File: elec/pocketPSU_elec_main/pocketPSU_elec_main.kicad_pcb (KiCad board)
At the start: 2 copper layers, 90 x 90 mm, 76 parts, among them J1 Header-Male-2.54_1x20, J2 Conn_01x03_Pin, J3 Conn_01x12_Pin, SW1 EC11E09244BS, SW3 TS-1187A-B-A-B, SW6 TS-1187A-B-A-B, U1 2N7002_C5224215, U2 ESP32-S3-WROOM-1(N16R2), U3 AMS1117-3.3, U4 FUSB302MPX, U5 F.0603.00026/P2-0603B1TS2-06T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

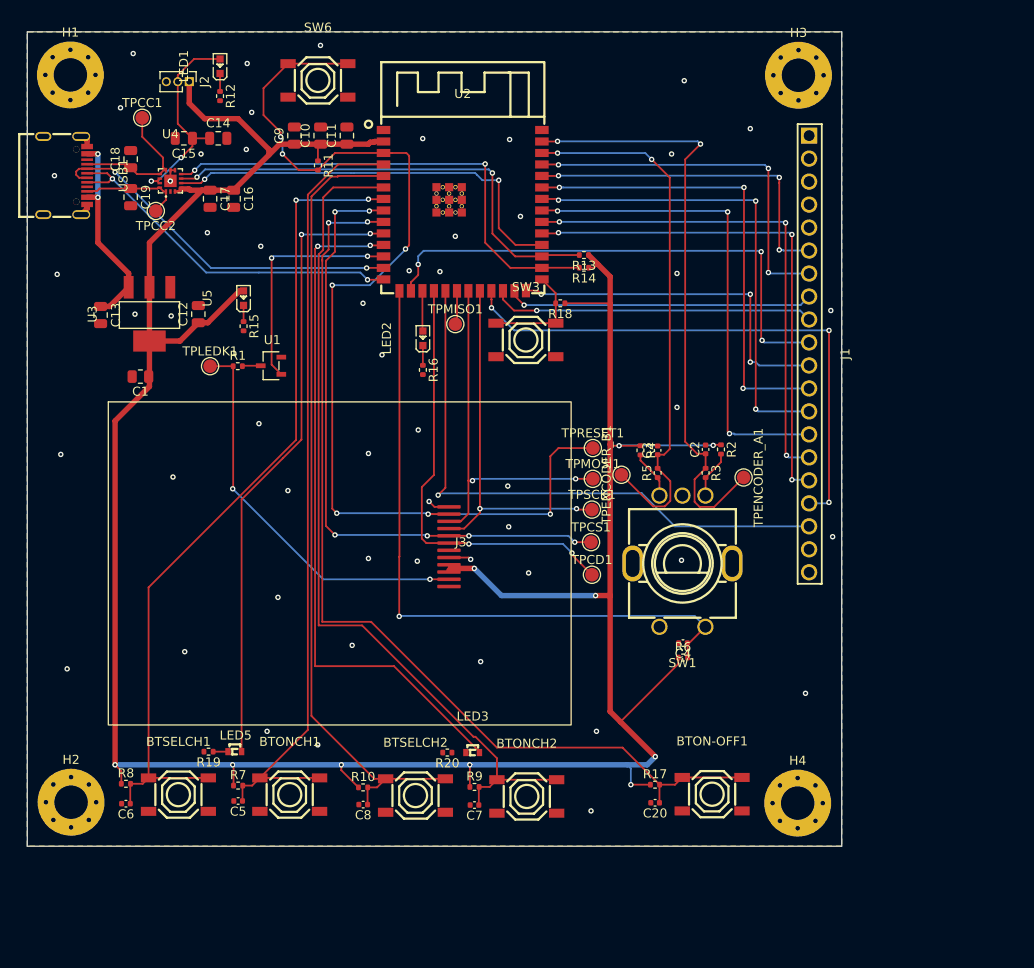
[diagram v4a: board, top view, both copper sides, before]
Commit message: Cleanup, Buck, CAN (#6)
* mid-layout

* finished routing

* Kibot (#7)

Add kibot with JLC output generation

* fix 3d, add drc

* fix erc

* fix pcb drc

* drc ignore_unconnected

* attempt to add githash and tag

* add silk githash string

* add silk tag string

* change outputs

---------

Co-authored-by: Jarrod Tuma <jtuma@Jarrods-Laptop.local>
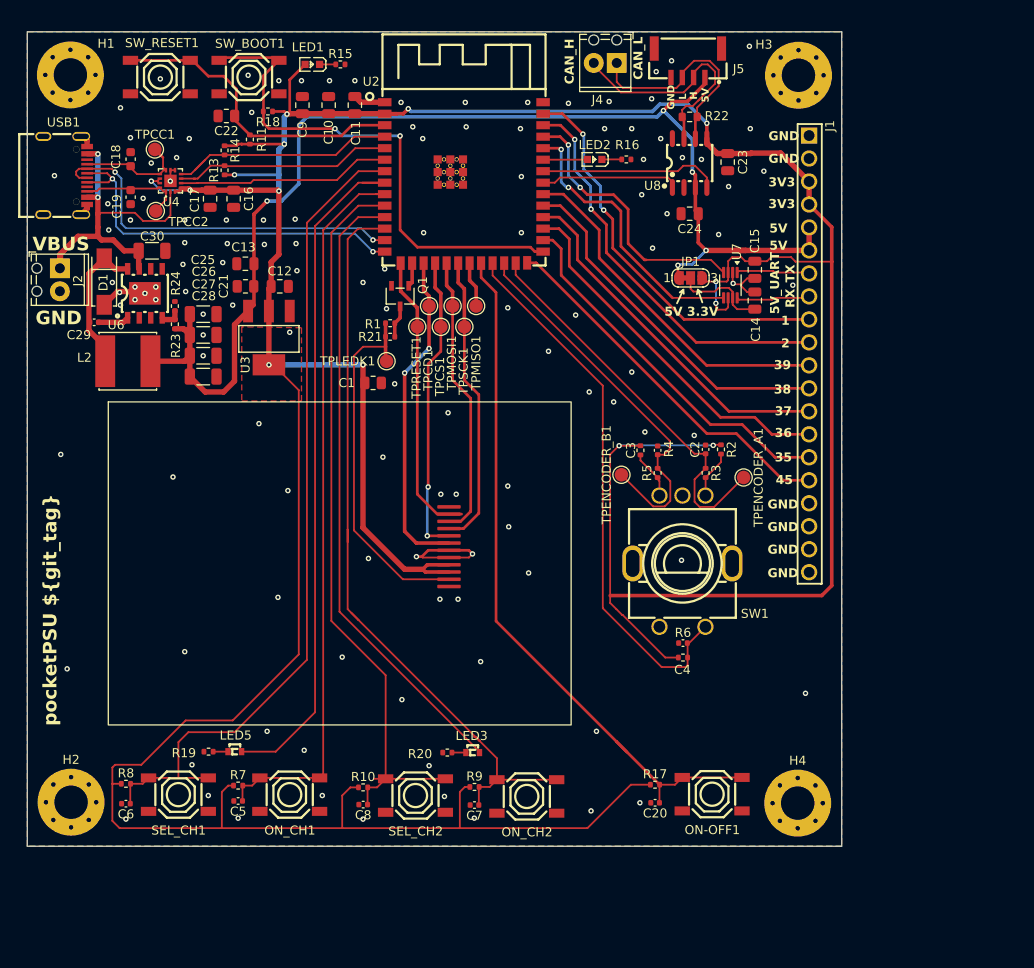
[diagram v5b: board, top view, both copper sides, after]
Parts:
- removed the LED1 at (118.9, 39.5)
- removed R12: 100R, Resistor_SMD:R_0402_1005Metric
- added C21: 1uF, Resistor_SMD:R_0805_2012Metric, F.Cu at (121.7, 63.8)
- added C22: 1uF, Resistor_SMD:R_0805_2012Metric, F.Cu at (119.6, 45.0)
- added C23: 100nF, Capacitor_SMD:C_0805_2012Metric, F.Cu at (175.0, 50.1)
- added C24: 100nF, Capacitor_SMD:C_0805_2012Metric, F.Cu at (170.8, 55.8)
- added C25: 47uF, Capacitor_SMD:C_1206_3216Metric, F.Cu at (117.0, 66.9)
- added C26: 47uF, Capacitor_SMD:C_1206_3216Metric, F.Cu at (117.0, 69.2)
- added C27: 47uF, Capacitor_SMD:C_1206_3216Metric, F.Cu at (117.0, 71.5)
- added C28: 47uF, Capacitor_SMD:C_1206_3216Metric, F.Cu at (117.0, 73.8)
- added C29: 10nF, Capacitor_SMD:C_0402_1005Metric, F.Cu at (105.0, 67.8)
- added C30: 4.7uF, Capacitor_SMD:C_1206_3216Metric, F.Cu at (111.4, 59.9)
- added D1: SS14, footprints:SMA_L4.2-W2.6-LS5.3-RD, F.Cu at (106.1, 63.3)
- added J4: Screw_Terminal_01x02, TerminalBlock_Phoenix:TerminalBlock_Phoenix_MPT-0,5-2-2.54_1x02_P2.54mm_Horizontal, F.Cu at (162.7, 39.1)
- added J5: SM04B-GHS-TB(LF)(SN), footprints:CONN-SMD_4P-P1.25_SM04B-GHS-TB-LF-SN, F.Cu at (170.6, 39.1)
- added JP1: SolderJumper_3_Bridged12, Jumper:SolderJumper-3_P1.3mm_Bridged12_RoundedPad1.0x1.5mm_NumberLabels, F.Cu at (170.9, 62.9)
- added L2: NRS6028T220MMGJV, footprints:IND-SMD_L6.0-W6.0, F.Cu at (108.7, 72.1)
- added R21: 10R, Resistor_SMD:R_0402_1005Metric, F.Cu at (137.7, 69.4)
- added R22: 120R, Resistor_SMD:R_0603_1608Metric, F.Cu at (170.8, 45.1)
- added R23: 10K, Resistor_SMD:R_0402_1005Metric, F.Cu at (113.9, 68.0)
- added R24: 3.3K, Resistor_SMD:R_0402_1005Metric, F.Cu at (113.9, 66.0)
- added U6: TPS5430DDAR, footprints:ESOP-8_L4.9-W3.9-P1.27-LS6.0-TL-EP, F.Cu at (110.6, 64.6)
- added U7: TXS0102DCU, Package_SO:VSSOP-8_2.3x2mm_P0.5mm, F.Cu at (175.3, 63.7)
- added U8: TJA1044GT/3Z, footprints:SO-8_L4.9-W3.9-P1.27-LS5.9-BL, F.Cu at (170.8, 50.2)
- C14: value 10uF -> 100nF
- C18, C19: value 300pF -> 330pF; footprint Capacitor_SMD:C_0805_2012Metric -> Capacitor_SMD:C_0603_1608Metric
- J2: value Conn_01x03_Pin -> Screw_Terminal_01x02; footprint Connector_PinHeader_1.27mm:PinHeader_1x03_P1.27mm_Vertical -> TerminalBlock_Phoenix:TerminalBlock_Phoenix_MPT-0,5-2-2.54_1x02_P2.54mm_Horizontal
- R1: value 4.7R -> 10R
- R3, R5: value 10K -> 100R
- moved C15 64.8 mm to (178.0, 62.0), turned to -90 degrees
- moved C14 62.0 mm to (178.0, 65.4), turned to 90 degrees
- moved SW_BOOT1 42.2 mm to (122.1, 40.7)
- moved R14 41.8 mm to (119.4, 48.8), turned to -90 degrees
- moved R13 40.8 mm to (119.4, 51.0), turned to 90 degrees
- moved R18 38.6 mm to (124.2, 44.5)
- moved TPCD1 34.7 mm to (142.0, 66.0)
- moved R16 32.4 mm to (163.8, 49.8), turned to 0 degrees
- moved R15 30.8 mm to (132.2, 39.3), turned to 0 degrees
- moved TPCS1 29.0 mm to (143.3, 68.3)
- moved LED2 27.4 mm to (160.3, 49.8), turned to 180 degrees
- moved LED1 26.9 mm to (129.1, 39.3), turned to 180 degrees
- moved C1 25.7 mm to (135.8, 74.5), turned to 0 degrees
- moved J2 25.1 mm to (101.2, 61.8)
- moved TPSCK1 24.6 mm to (145.9, 68.3)
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- renumbered U5 to LED1, BTON-OFF1 to ON-OFF1, BTONCH1 to ON_CH1, BTONCH2 to ON_CH2, U1 to Q1, BTSELCH1 to SEL_CH1, BTSELCH2 to SEL_CH2, SW3 to SW_BOOT1, SW6 to SW_RESET1
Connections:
- C13 pad 1: VBUS -> +5V
- C14 pad 1: /usb_input/USB_VCONN -> Net-(JP1-C)
- C15 pad 1: /usb_input/USB_VCONN -> +3.3V
- C5 pad 1: /microcontroller/BT_SEL_CH1 -> /microcontroller/BT_ON_CH1
- C6 pad 1: /microcontroller/BT_ON_CH2 -> /microcontroller/BT_SEL_CH1
- C7 pad 1: /microcontroller/BT_SEL_CH2 -> /microcontroller/BT_ON_CH2
- C8 pad 1: /microcontroller/BT_ON_CH1 -> /microcontroller/BT_SEL_CH2
- J1 pad 1: unconnected-(J1-Pad1) -> GND
- J1 pad 10: /microcontroller/IO46 -> /microcontroller/IO2
- J1 pad 11: /microcontroller/IO45 -> /microcontroller/IO39
- J1 pad 12: /microcontroller/IO42 -> /microcontroller/IO38
- J1 pad 13: /microcontroller/IO41 -> /microcontroller/IO37
- J1 pad 14: /microcontroller/IO40 -> /microcontroller/IO36
- J1 pad 15: /microcontroller/IO39 -> /microcontroller/IO35
- J1 pad 16: /microcontroller/IO38 -> /microcontroller/IO45
- J1 pad 17: /microcontroller/IO21 -> GND
- J1 pad 18: /microcontroller/IO11 -> GND
- J1 pad 19: /microcontroller/IO18 -> GND
- J1 pad 2: unconnected-(J1-Pad2) -> GND
- J1 pad 20: /microcontroller/IO17 -> GND
- J1 pad 3: unconnected-(J1-Pad3) -> +3.3V
- J1 pad 4: unconnected-(J1-Pad4) -> +3.3V
- J1 pad 5: unconnected-(J1-Pad5) -> +5V
- J1 pad 6: /microcontroller/RXD0 -> +5V
- J1 pad 7: /microcontroller/TXD0 -> /microcontroller/TX_5V
- J1 pad 8: /microcontroller/IO48 -> /microcontroller/RX_5V
- J1 pad 9: /microcontroller/IO47 -> /microcontroller/IO1
- J2 pad 1: +3.3V -> VBUS
- J2 pad 2: /usb_input/USB_VCONN -> GND
- ON_CH1 pad 1: /microcontroller/BT_SEL_CH1 -> /microcontroller/BT_ON_CH1
- ON_CH1 pad 2: /microcontroller/BT_SEL_CH1 -> /microcontroller/BT_ON_CH1
- ON_CH2 pad 1: /microcontroller/BT_SEL_CH2 -> /microcontroller/BT_ON_CH2
- ON_CH2 pad 2: /microcontroller/BT_SEL_CH2 -> /microcontroller/BT_ON_CH2
- R10 pad 2: /microcontroller/BT_ON_CH1 -> /microcontroller/BT_SEL_CH2
- R11 pad 2: /user_interface/SPI_RESET -> Net-(SW_RESET1-A)
- R7 pad 2: /microcontroller/BT_SEL_CH1 -> /microcontroller/BT_ON_CH1
- R8 pad 2: /microcontroller/BT_ON_CH2 -> /microcontroller/BT_SEL_CH1
- R9 pad 2: /microcontroller/BT_SEL_CH2 -> /microcontroller/BT_ON_CH2
- SEL_CH1 pad 1: /microcontroller/BT_ON_CH2 -> /microcontroller/BT_SEL_CH1
- SEL_CH1 pad 2: /microcontroller/BT_ON_CH2 -> /microcontroller/BT_SEL_CH1
- SEL_CH2 pad 1: /microcontroller/BT_ON_CH1 -> /microcontroller/BT_SEL_CH2
- SEL_CH2 pad 2: /microcontroller/BT_ON_CH1 -> /microcontroller/BT_SEL_CH2
- SW_RESET1 pad 1: /user_interface/SPI_RESET -> Net-(SW_RESET1-A)
- SW_RESET1 pad 2: /user_interface/SPI_RESET -> Net-(SW_RESET1-A)
- U2 pad 10: /microcontroller/CH1_LED -> /microcontroller/BT_SEL_CH2
- U2 pad 12: /user_interface/BACKLIGHT_EN -> /microcontroller/BT_ON_CH2
- U2 pad 15: /microcontroller/ENCODER_BT -> /user_interface/SPI_RESET
- U2 pad 16: /microcontroller/IO46 -> /user_interface/BACKLIGHT_EN
- U2 pad 17: /microcontroller/BLINKY_LED -> /user_interface/SPI_DC
- U2 pad 18: /user_interface/SPI_DC -> /user_interface/SPI_CS
- U2 pad 19: /microcontroller/IO11 -> /user_interface/SPI_MOSI
- U2 pad 20: /user_interface/SPI_MISO -> /user_interface/SPI_SCK
- U2 pad 21: /user_interface/SPI_MOSI -> /user_interface/SPI_MISO
- U2 pad 22: /user_interface/SPI_SCK -> /microcontroller/BT_ON_OFF
- U2 pad 23: /microcontroller/IO21 -> /microcontroller/ENCODER_BT
- U2 pad 24: /microcontroller/IO47 -> /microcontroller/ENCODER_B
- U2 pad 25: /microcontroller/IO48 -> /microcontroller/ENCODER_A
- U2 pad 28: /USB_SDA -> /microcontroller/IO35
- U2 pad 29: /USB_SCL -> /microcontroller/IO36
- U2 pad 3: /user_interface/SPI_RESET -> Net-(SW_RESET1-A)
- U2 pad 30: /USB_INT_N -> /microcontroller/IO37
- U2 pad 33: /microcontroller/IO40 -> /microcontroller/CAN_TX
- U2 pad 34: /microcontroller/IO41 -> /microcontroller/CAN_RX
- U2 pad 35: /microcontroller/IO42 -> /microcontroller/BLINKY_LED
- U2 pad 38: /microcontroller/ENCODER_B -> /microcontroller/IO2
- U2 pad 39: /microcontroller/ENCODER_A -> /microcontroller/IO1
- U2 pad 4: /microcontroller/BT_SEL_CH1 -> /USB_SDA
- U2 pad 5: /microcontroller/BT_ON_CH1 -> /USB_SCL
- U2 pad 6: /microcontroller/BT_SEL_CH2 -> /USB_INT_N
- U2 pad 7: /microcontroller/BT_ON_CH2 -> /microcontroller/BT_SEL_CH1
- U2 pad 8: /user_interface/SPI_CS -> /microcontroller/CH1_LED
- U2 pad 9: /microcontroller/BT_ON_OFF -> /microcontroller/BT_ON_CH1
- U3 pad 3: VBUS -> +5V
- U4 pad 12: /usb_input/USB_VCONN -> +3.3V
- U4 pad 13: /usb_input/USB_VCONN -> +3.3V
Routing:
- net +3.3V: track 305.6 -> 454.8 mm, vias 10 -> 14
- net +5V: track 0.00 -> 137.0 mm, vias 0 -> 5
- net /user_interface/SPI_RESET: track 118.2 -> 32.1 mm, vias 7 -> 0
- net /microcontroller/IO11: track 65.5 -> 0.00 mm, vias 1 -> 0
- net /microcontroller/IO21: track 61.5 -> 0.00 mm, vias 3 -> 0
- net /microcontroller/IO46: track 57.5 -> 0.00 mm, vias 3 -> 0
- net /microcontroller/IO40: track 54.0 -> 0.00 mm, vias 3 -> 0
- net /microcontroller/IO41: track 52.7 -> 0.00 mm, vias 3 -> 0
- net /microcontroller/IO42: track 51.9 -> 0.00 mm, vias 3 -> 0
- net Net-(SW_BOOT1-A): track 12.1 -> 57.4 mm, vias 0 -> 2
- net /microcontroller/IO2: track 0.00 -> 44.6 mm, vias 0 -> 2
- net /microcontroller/IO1: track 0.00 -> 44.3 mm, vias 0 -> 2
- net /microcontroller/IO35: track 0.00 -> 41.1 mm
- net /microcontroller/IO36: track 0.00 -> 40.6 mm
- net /microcontroller/IO37: track 0.00 -> 39.9 mm
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- added copper zone on F.Cu, net +3.3V
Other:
- board text added: "1"
- board text added: "2"
- board text added: "35"
- board text added: "36"
- board text added: "37"
- board text added: "38"
- board text added: "39"
- board text added: "3V3"
- board text added: "45"
- board text added: "5V"
- board text added: "5V 3.3V"
- board text added: "5V_UART"
- board text added: "CAN_H"
- board text added: "CAN_L"
- board text added: "GND"
- board text added: "H"
- board text added: "L"
- board text added: "RX"
- board text added: "TX"
- board text added: "VBUS"
- board text added: "pocketPSU ${git_tag}"

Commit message: Add mini esp32 module, smd rotary encoder and leds
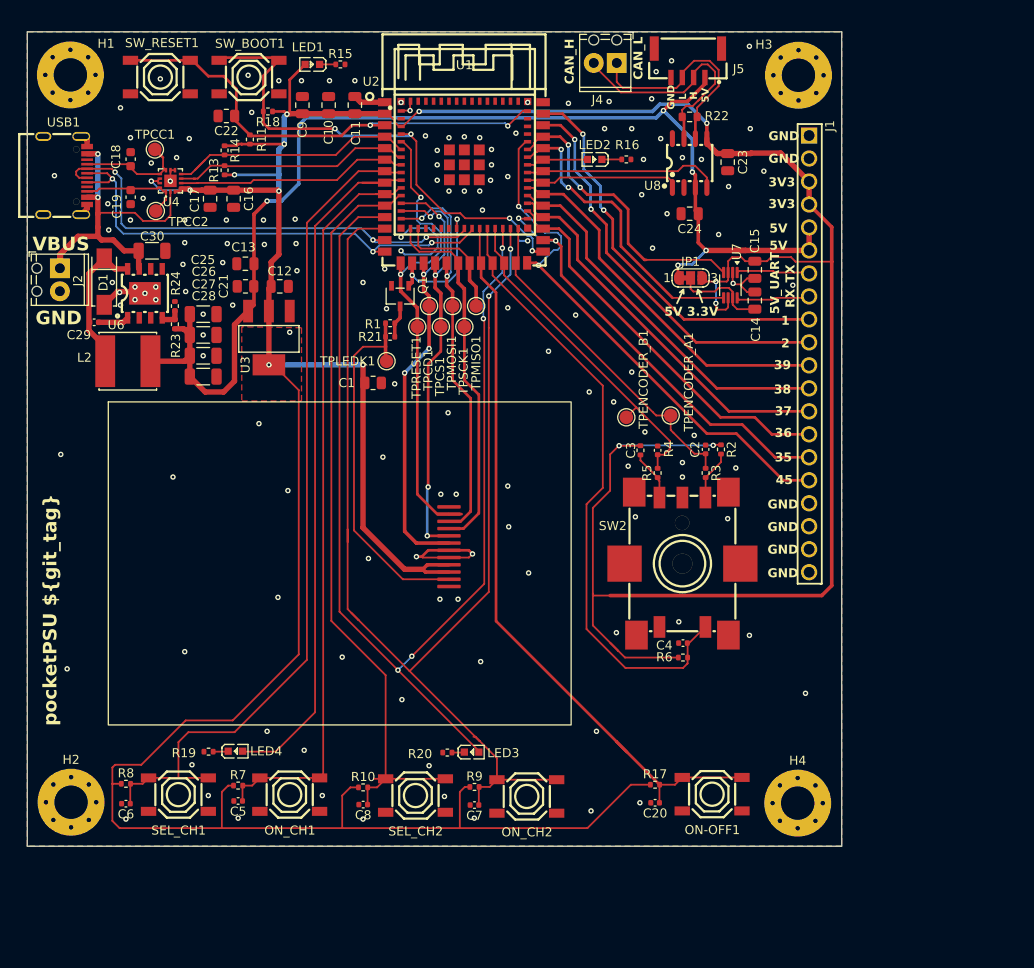
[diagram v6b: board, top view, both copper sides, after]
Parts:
- removed LED5: XL-1606SYGC, footprints:LED-SMD_L1.7-W1.1-RD_27-21
- removed SW1: EC11E09244BS, footprints:SW-TH_EC11XXXXXXXX
- added LED4: F.0603.00026/P2-0603B1TS2-06T-001, footprints:LED0603-RD, F.Cu at (120.6, 115.2)
- added SW2: EC11J1525402, footprints:SW-SMD_EC11J1525402, F.Cu at (170.0, 94.5)
- added U1: ESP32-S3-MINI-1-N4R2, footprints:BULETM-SMD_ESP32-S3-MINI-1-N8, F.Cu at (145.9, 50.4)
- LED3: value XL-1606SYGC -> F.0603.00026/P2-0603B1TS2-06T-001; footprint footprints:LED-SMD_L1.7-W1.1-RD_27-21 -> footprints:LED0603-RD
- moved TPENCODER_A1 10.6 mm to (168.7, 78.1)
- moved TPENCODER_B1 6.37 mm to (163.8, 78.3)
- moved LED3 0.13 mm to (146.7, 115.3)
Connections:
- net Net-(SW_BOOT1-A) renamed /microcontroller/BOOT
- net Net-(SW_RESET1-A) renamed /microcontroller/EN
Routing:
- net /microcontroller/CH2_LED: track 69.4 -> 123.1 mm, vias 0 -> 4
- net /microcontroller/BT_ON_CH2: track 85.5 -> 139.1 mm, vias 0 -> 2
- net /user_interface/SPI_RESET: track 32.1 -> 52.7 mm, vias 0 -> 2
- net /microcontroller/EN: track 34.2 -> 52.4 mm, vias 0 -> 2
- net /microcontroller/IO45: track 41.1 -> 59.3 mm, vias 0 -> 2
- net GND: track 31.4 -> 45.2 mm, vias 124 -> 144
- net /user_interface/SPI_MOSI: track 31.4 -> 44.5 mm, vias 0 -> 2
- net /user_interface/SPI_CS: track 33.4 -> 46.3 mm, vias 2 -> 4
- net /user_interface/BACKLIGHT_EN: track 2.67 -> 15.3 mm, vias 0 -> 2
- net /user_interface/SPI_DC: track 36.4 -> 48.9 mm, vias 2 -> 4
- net /USB_DP: track 42.3 -> 54.5 mm, vias 2 -> 3
- net /USB_DM: track 42.1 -> 53.1 mm, vias 2 -> 3
- net /user_interface/SPI_MISO: track 5.04 -> 13.7 mm
- net /user_interface/SPI_SCK: track 32.6 -> 40.6 mm
- net /microcontroller/ENCODER_BT: track 60.5 -> 68.5 mm
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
